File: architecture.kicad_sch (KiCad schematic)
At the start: 0 parts

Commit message: sensors done, mcu worked on
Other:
- added sheet Sensors (sensors.kicad_sch)
- title: Hoppen FC -> MCU Power
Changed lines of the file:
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@@
 	(paper "A4")
 	(title_block
-		(title "Hoppen FC")
+		(title "MCU Power")
 		(date "2025-12-13")
 		(rev "1.0")
@@
 	)
 	(sheet
+		(at 73.66 71.12)
+		(size 12.7 3.81)
+		(exclude_from_sim no)
+		(in_bom yes)
+		(on_board yes)
+		(dnp no)
+		(fields_autoplaced yes)
+		(stroke
+			(width 0.1524)
+			(type solid)
+		)
+		(fill
+			(color 0 0 0 0.0000)
+		)
+		(property "Sheetname" "Sensors"
+			(at 73.66 70.4084 0)
+			(effects
+				(font
+					(size 1.27 1.27)
+				)
+				(justify left bottom)
+			)
+		)
+		(property "Sheetfile" "sensors.kicad_sch"
+			(at 73.66 75.5146 0)
+			(effects
+				(font
+					(size 1.27 1.27)
+				)
+				(justify left top)
+			)
+		)
+		(instances
+			(project "hoppen_fc"
+				(path "/abe950a1-9eef-4508-9fd4-31d3e723e029/c85454e5-a89e-41eb-a5ed-71b4fc4cf13a"
+					(page "6")
+				)
+			)
+		)
+	)
+	(sheet

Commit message: rs232,can,ind,storage,usb v01
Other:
- added sheet CAN (canbus.kicad_sch)
- added sheet Indicators (indicators.kicad_sch)
- added sheet Interfaces (interface.kicad_sch)
- added sheet Misc (misc.kicad_sch)
- added sheet Power (power.kicad_sch)
- added sheet Power Input (power_input.kicad_sch)
- added sheet RS232 (rs232.kicad_sch)
- added sheet Storage (storage.kicad_sch)
- added sheet USB (usb.kicad_sch)

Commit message: wen branch and pr
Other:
- sheet CAN renamed FDCAN
- removed sheet Power Input
- added sheet Radio (radio.kicad_sch)
- sheet FDCAN ports: added {FDCAN1_TTL}, {FDCAN1}, {FDCAN2_TTL}, {FDCAN2}; removed none
- sheet Indicators ports: added ADD_LED, BUZZER, DBG_LED_1, DBG_LED_2; removed none
- sheet Power ports: added +3V3, +5V, +5V_EXT, +BAT, +BAT_PROT, +BAT_VMON, BATTERY_IMON, BAT_PG; removed none
- sheet RS232 ports: added RS232_nEN, RS232_nSHDN, {RS232_IN}, {VN_RS232}; removed none
- sheet Sensors ports: added BARO_CS, IMU_ACC_CS, IMU_GYRO_CS, INT1_ACC, INT3_GYRO, MAG_CS, MAG_INT, {SPI4}, {SPI5}; removed none
- sheet Storage ports: added CARD_DETECT, {QSPI}, {SD}; removed none
- sheet USB ports: added VBUS_MON, {USB}; removed none
- title: MCU Power -> Architecture

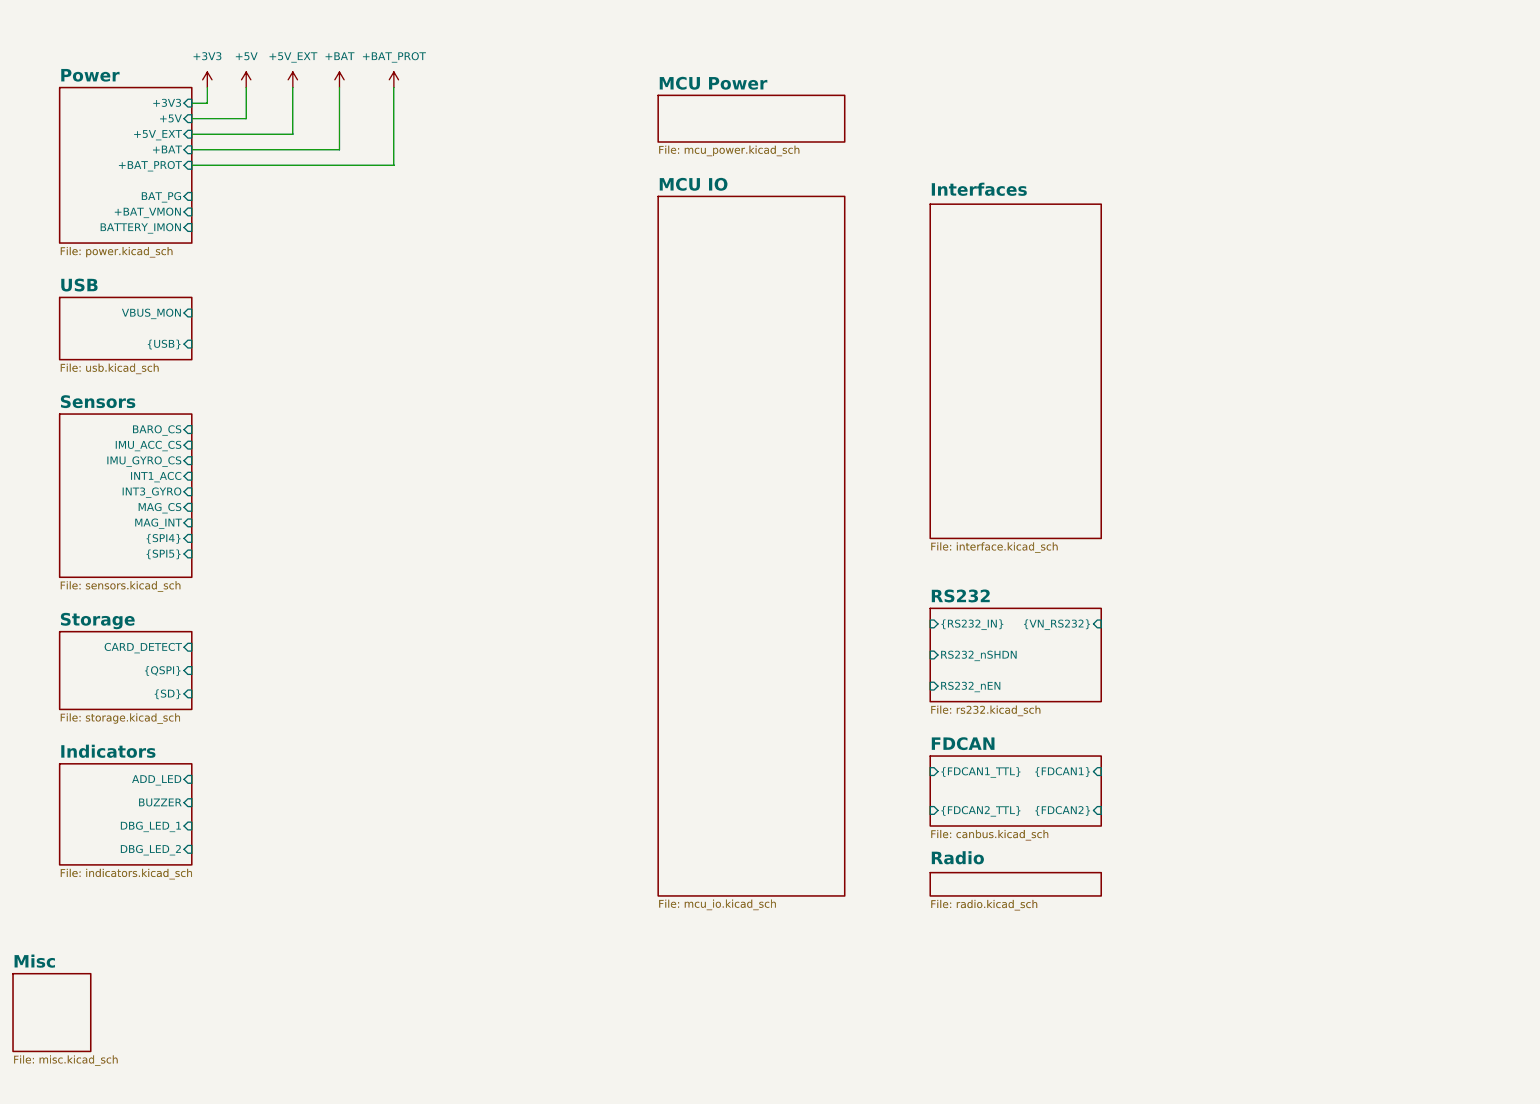
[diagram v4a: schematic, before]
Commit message: much work and .ioc file added
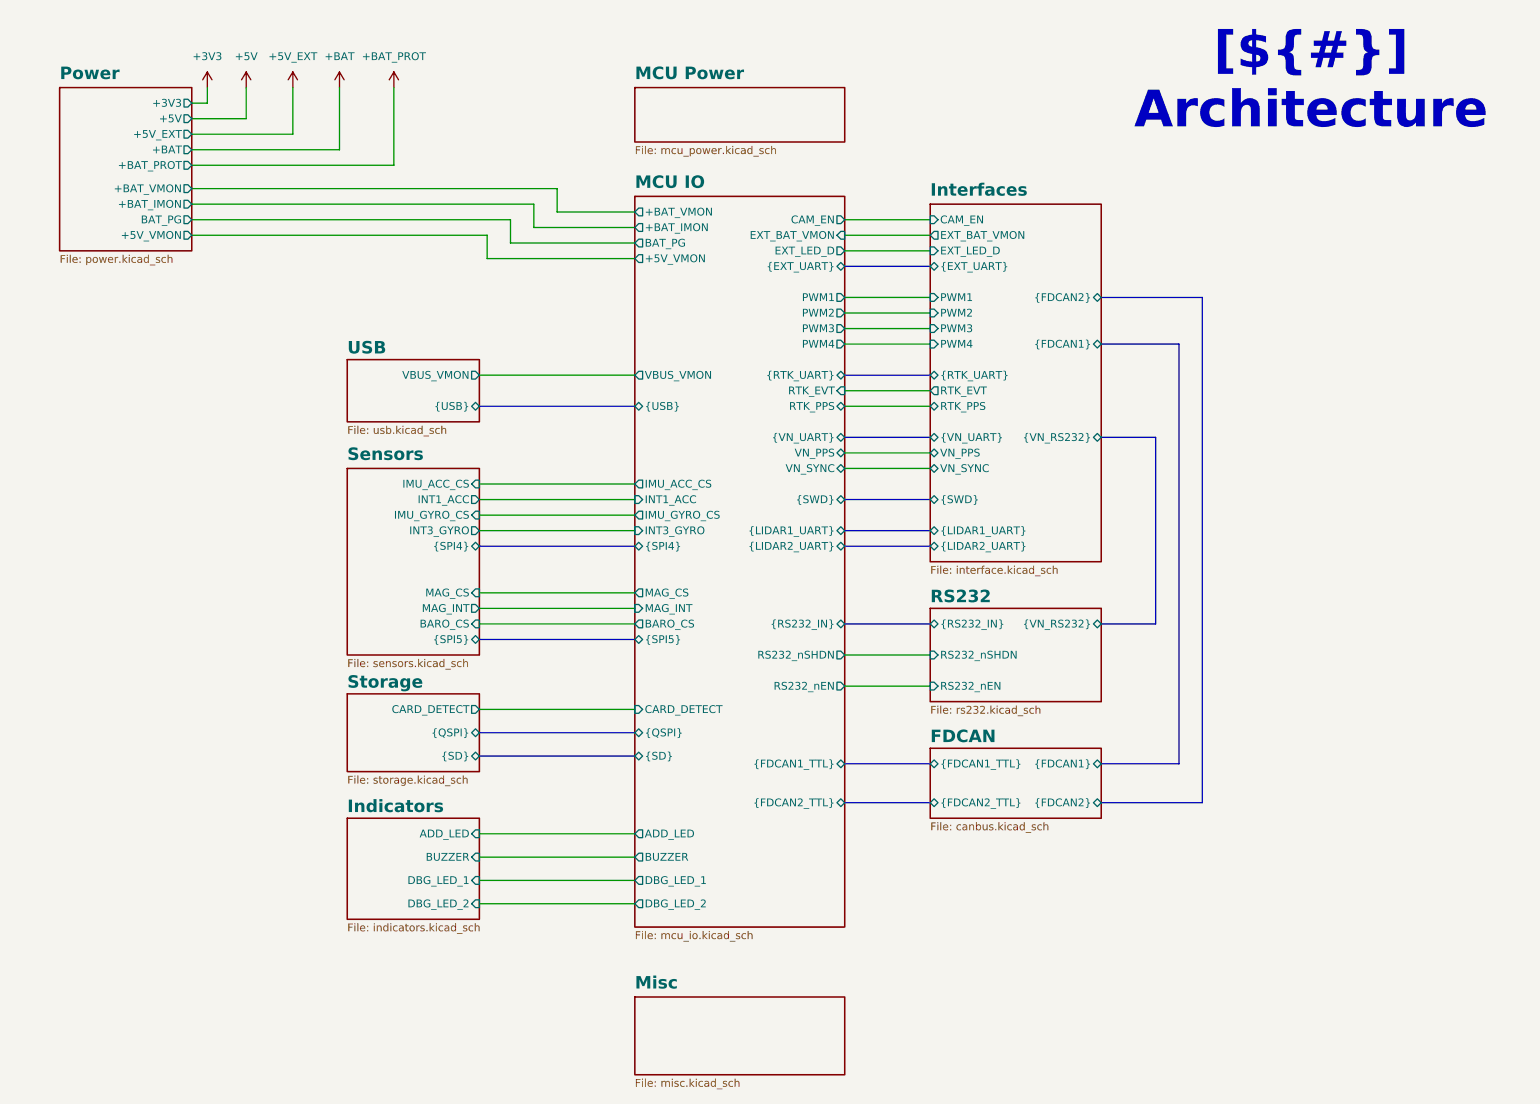
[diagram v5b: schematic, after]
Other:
- removed sheet Radio
- sheet Interfaces ports: added CAM_EN, EXT_BAT_VMON, EXT_LED_D, PWM1, PWM2, PWM3, PWM4, RTK_EVT, RTK_PPS, VN_PPS, VN_SYNC, {EXT_UART}, {FDCAN1}, {FDCAN2}, {LIDAR1_UART}, {LIDAR2_UART}, {RTK_UART}, {SWD}, {VN_RS232}, {VN_UART}; removed none
- sheet MCU IO ports: added +5V_VMON, +BAT_IMON, +BAT_VMON, ADD_LED, BARO_CS, BAT_PG, BUZZER, CAM_EN, CARD_DETECT, DBG_LED_1, DBG_LED_2, EXT_BAT_VMON, EXT_LED_D, IMU_ACC_CS, IMU_GYRO_CS, INT1_ACC, INT3_GYRO, MAG_CS, MAG_INT, PWM1, PWM2, PWM3, PWM4, RS232_nEN, RS232_nSHDN, RTK_EVT, RTK_PPS, VBUS_VMON, VN_PPS, VN_SYNC, {EXT_UART}, {FDCAN1_TTL}, {FDCAN2_TTL}, {LIDAR1_UART}, {LIDAR2_UART}, {QSPI}, {RS232_IN}, {RTK_UART}, {SD}, {SPI4}, {SPI5}, {SWD}, {USB}, {VN_UART}; removed none
- sheet Power ports: added +5V_VMON, +BAT_IMON; removed BATTERY_IMON
- sheet USB ports: added VBUS_VMON; removed VBUS_MON
